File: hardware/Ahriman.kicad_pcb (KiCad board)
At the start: 4 copper layers, 52.7 x 61.5 mm, 112 parts, among them J1 Power_In, J10 USB3145-30-1-A, J2 SWD_Debug, J3 UART_Debug, J4 POT1, J5 PB_Foot, J6 POT2, J7 POT3, J8 Analog_In, J9 Analog_Out, Q1 T2N7002AK, Q2 T2N7002AK, Q3 T2N7002AK, SW1 PTS636, U1 EFM32TG11B520F128GM64-A, U2 NE5532, U3 UA78M33CKVURG3, U4 GD25Q80CSIGR, U5 NAU88C10YG, U6 AD8034ARZ, U7 74AHC1G14, U8 SP0503BAHTG, U9 CP2110-F01-GM, Y1 12.0MHz

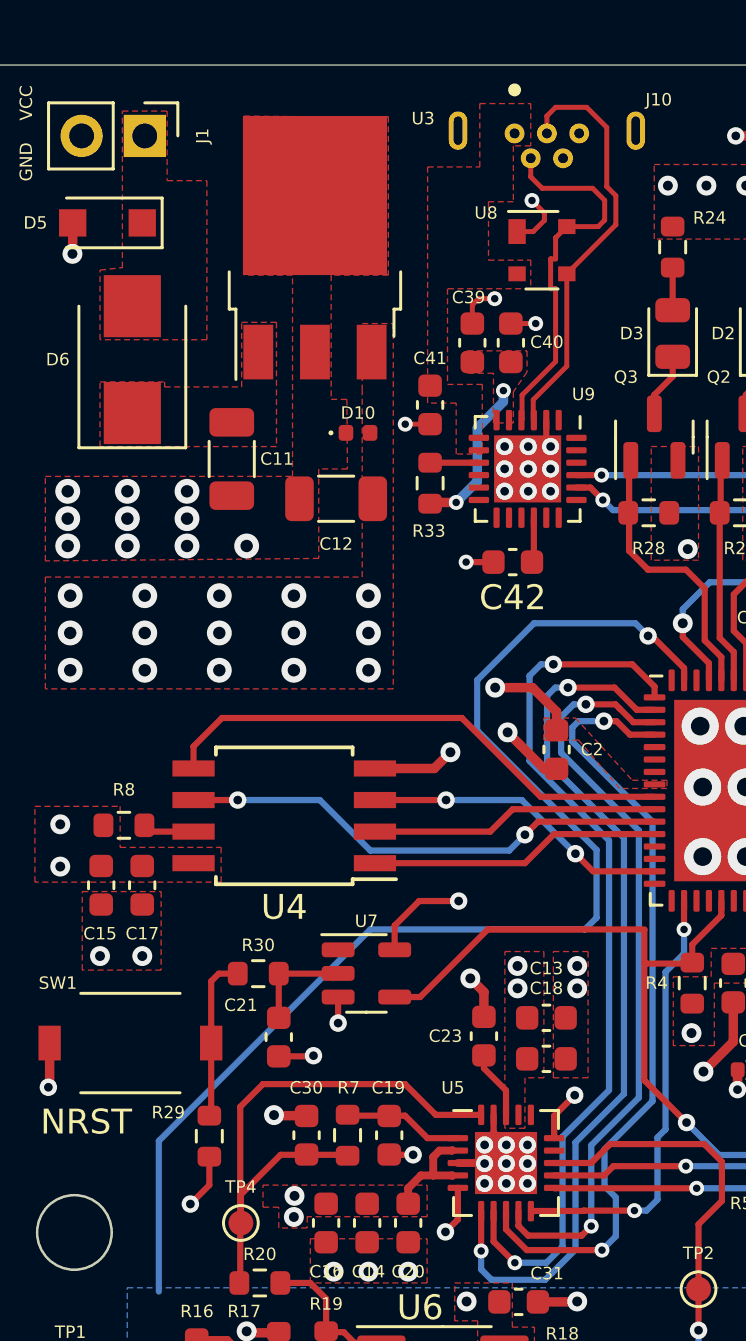
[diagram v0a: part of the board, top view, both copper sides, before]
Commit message: Re-organize File Structure
Start ignoring unwanted files
Create BOM
Re-organize files
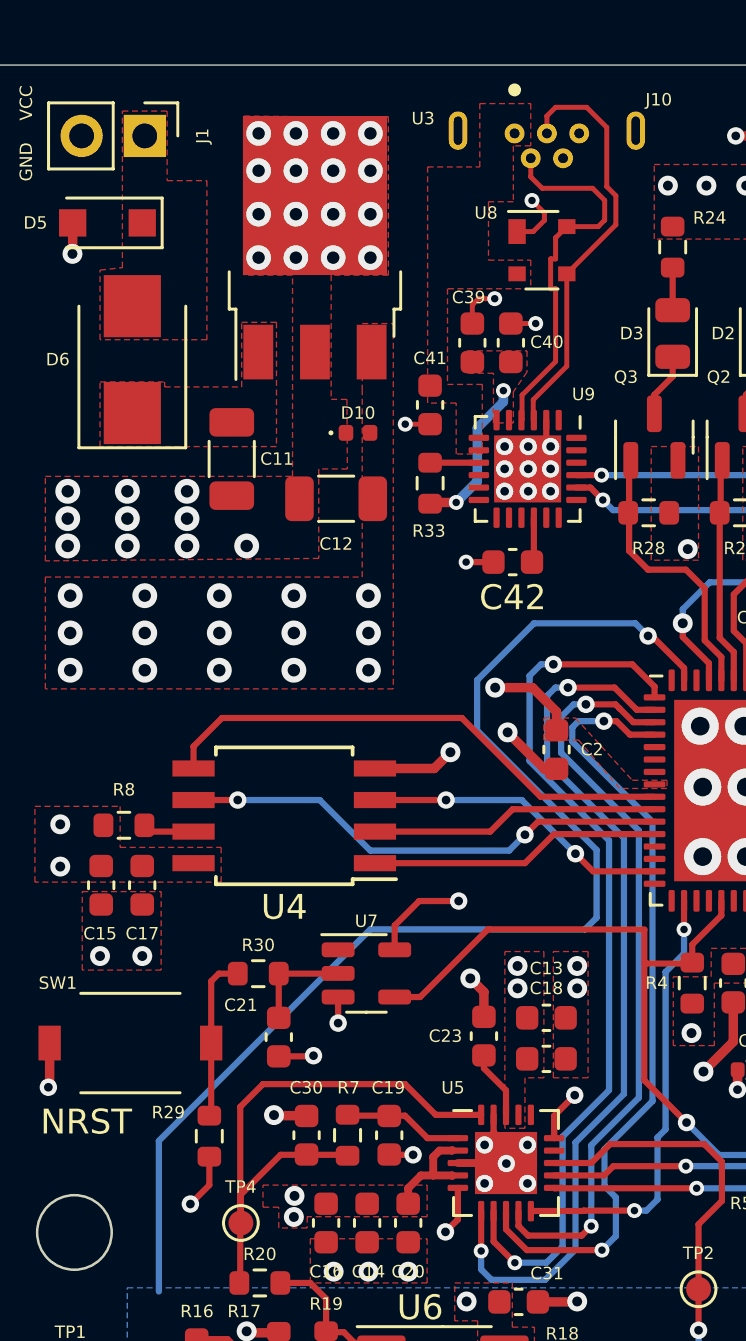
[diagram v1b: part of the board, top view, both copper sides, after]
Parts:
- R26, R27, R28: value 50 -> 10k
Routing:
- net GND: vias 97 -> 109
